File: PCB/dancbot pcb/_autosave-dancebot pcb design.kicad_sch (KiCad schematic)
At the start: 26 parts, among them J1 ESP32-PICO-KIT-V4.1, J2 Voltage Regulator, J4 Pins, J6 Conn_01x04_Socket, J7 Conn_01x04_Socket, Q1 PMOS, Q2 PMOS, Q3 2N3904, Q5 PMOS, SW1 SP switch, SW2 SW_SPST

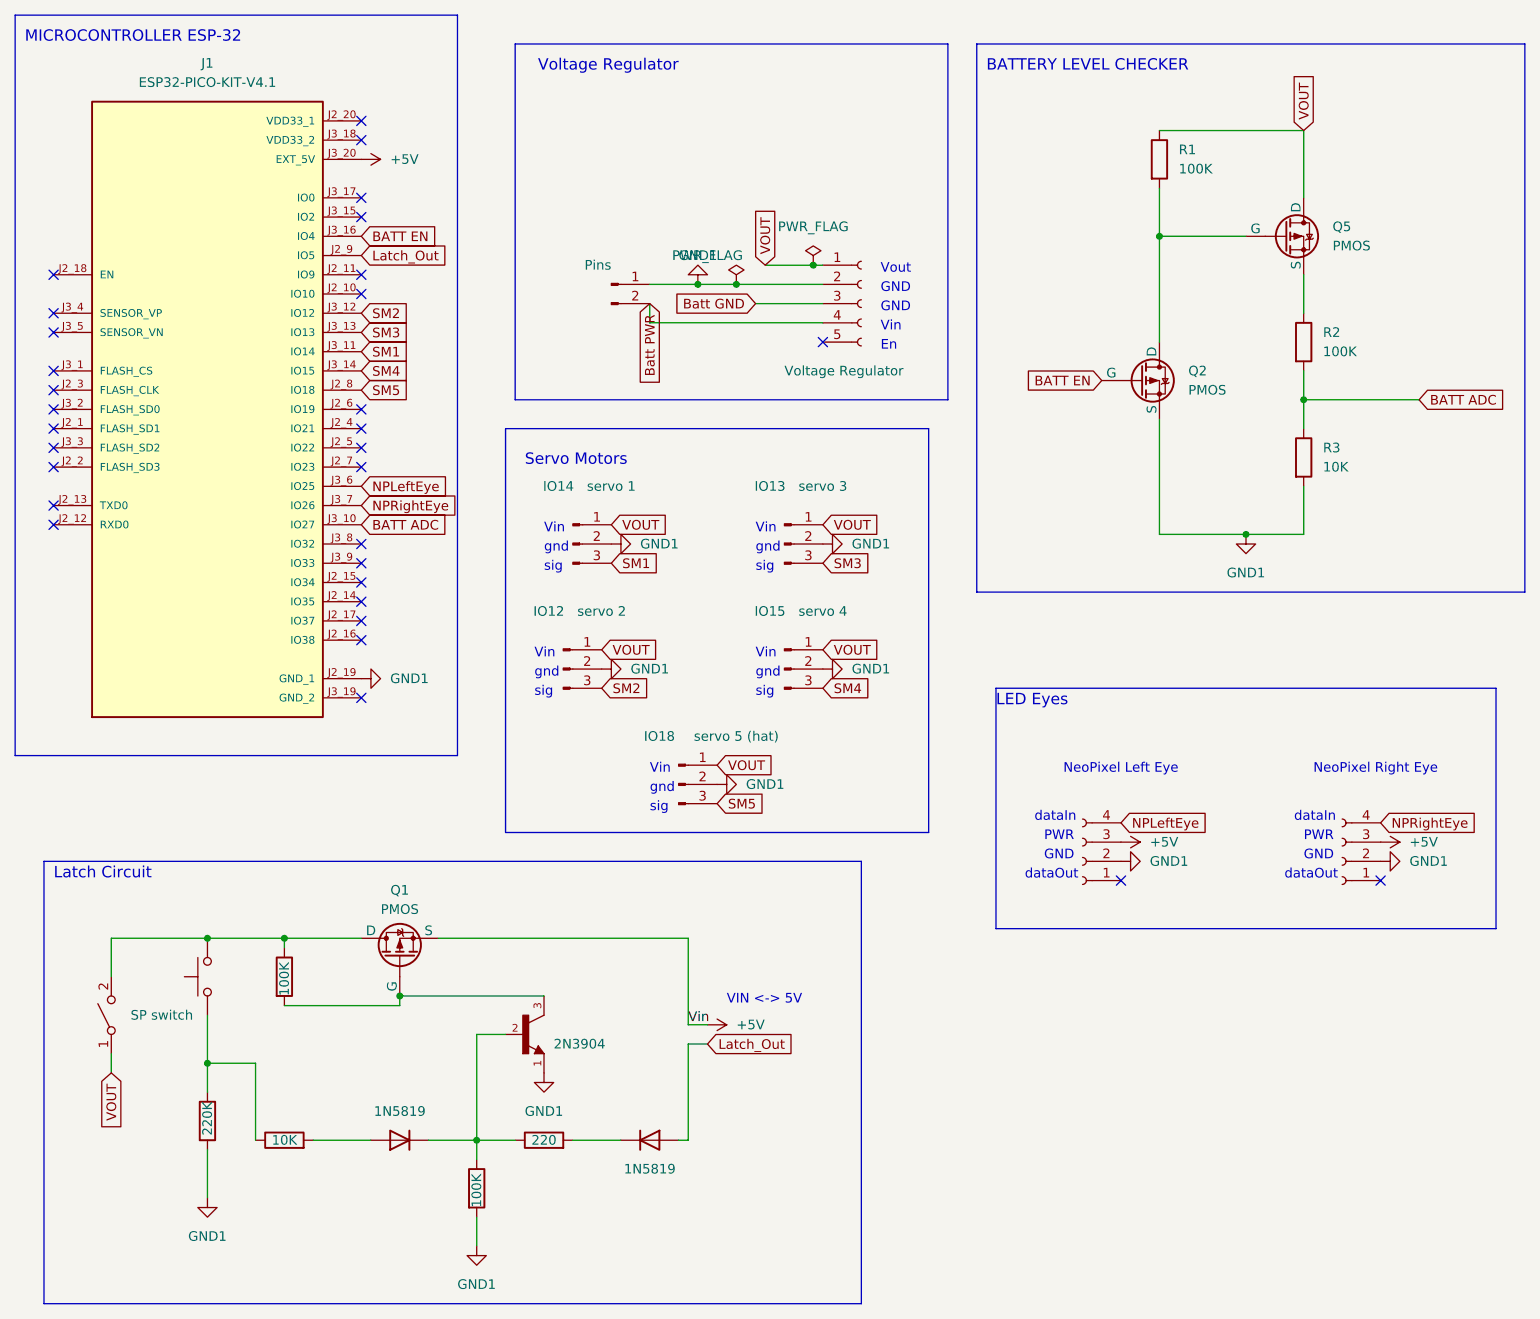
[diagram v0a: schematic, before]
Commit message: Routing rev5, fixed batt lvl checker, fixed gnd plane
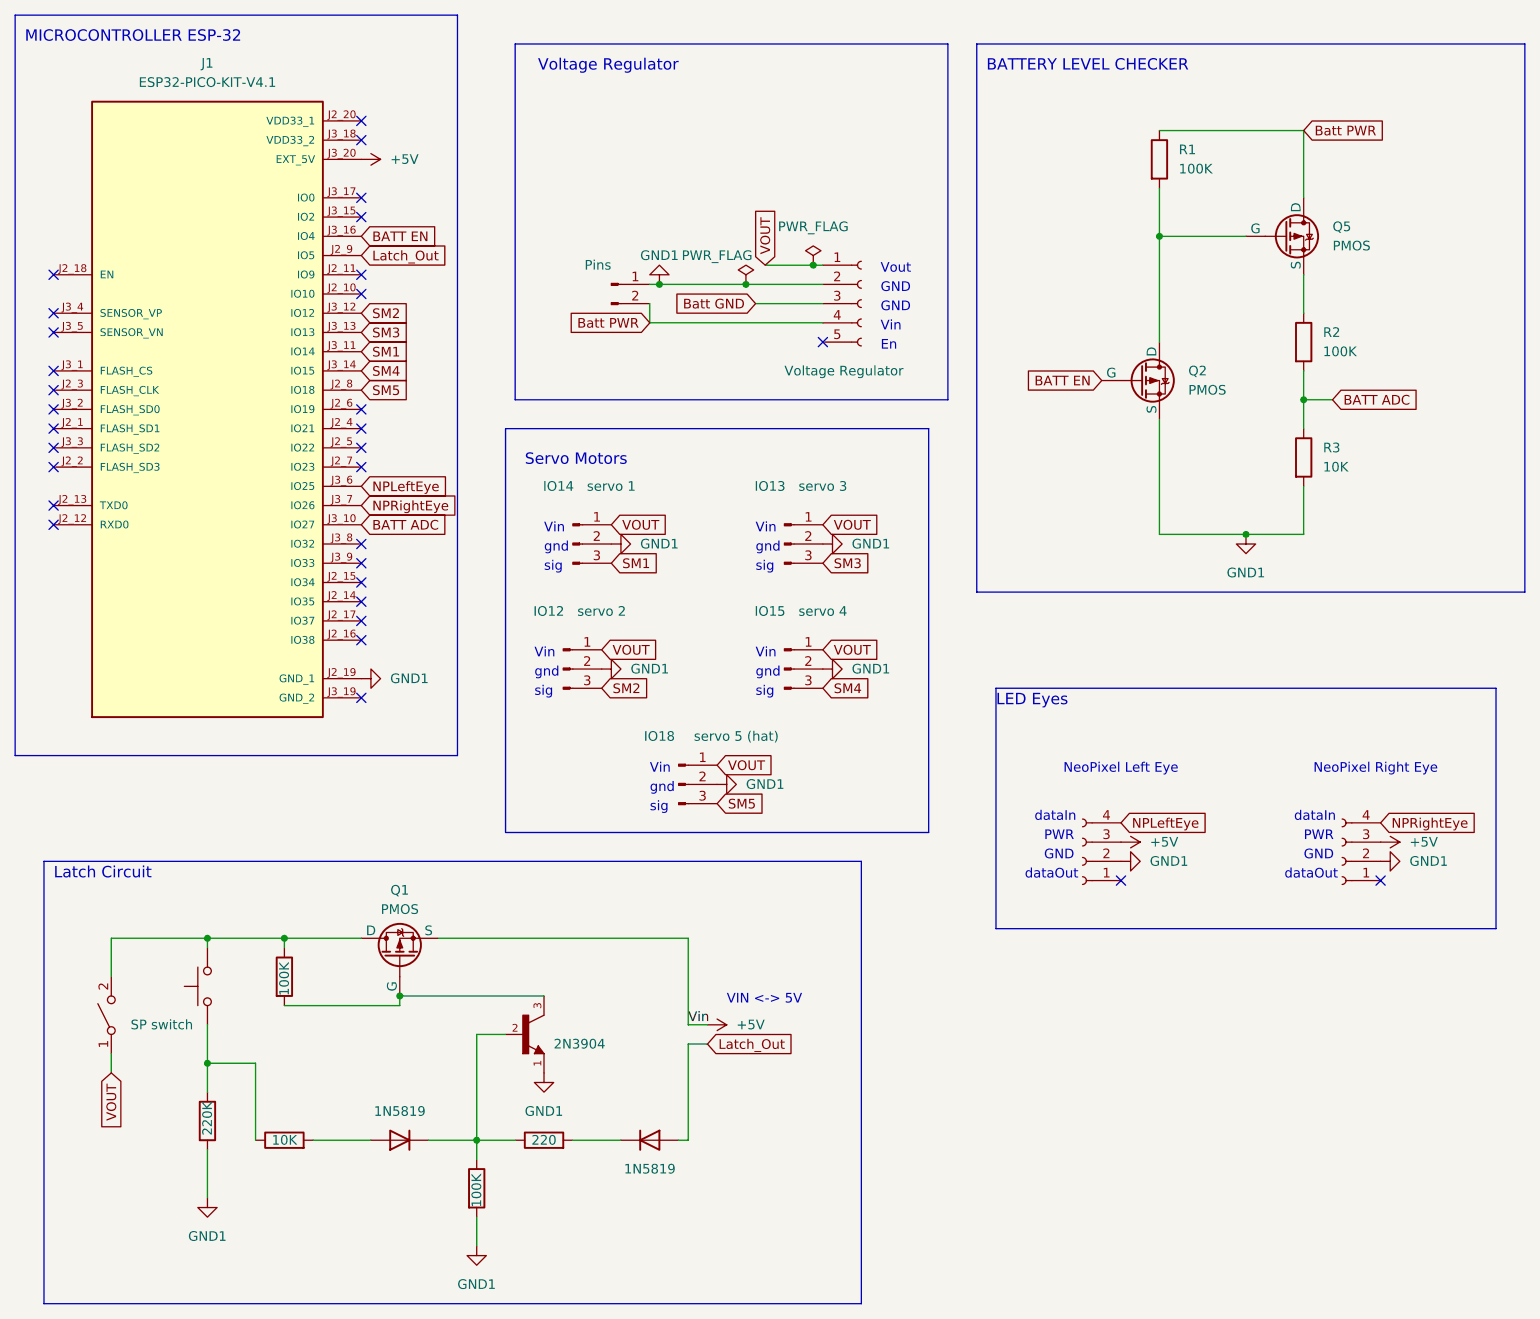
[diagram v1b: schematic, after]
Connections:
- net Batt PWR: now also Q5.1 (D), R1.1
- net VOUT: no longer Q5.1 (D), R1.1
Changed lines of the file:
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@@
 (kicad_sch (version 20230121) (generator eeschema)
   (paper "A4")
-  (junction (at 111.76 50.8) (diameter 0) (color 0 0 0 0)
-  )
   (junction (at 179.07 83.82) (diameter 0) (color 0 0 0 0)
   )
@@
   (junction (at 41.91 153.67) (diameter 0) (color 0 0 0 0)
   )
-  (junction (at 106.68 50.8) (diameter 0) (color 0 0 0 0)
+  (junction (at 113.03 50.8) (diameter 0) (color 0 0 0 0)
+  )
+  (junction (at 101.6 50.8) (diameter 0) (color 0 0 0 0)
   )
   (junction (at 52.07 137.16) (diameter 0) (color 0 0 0 0)
@@
     (stroke (width 0) (type default))
   )
+  (wire (pts (xy 41.91 138.43) (xy 41.91 137.16))
+    (stroke (width 0) (type default))
+  )
   (wire (pts (xy 77.47 163.83) (xy 77.47 149.86))
     (stroke (width 0) (type default))
@@
     (stroke (width 0) (type default))
   )
-  (wire (pts (xy 106.68 50.8) (xy 111.76 50.8))
-    (stroke (width 0) (type default))
-  )
   (wire (pts (xy 41.91 153.67) (xy 48.26 153.67))
     (stroke (width 0) (type default))
@@
     (stroke (width 0) (type default))
   )
+  (wire (pts (xy 113.03 50.8) (xy 123.19 50.8))
+    (stroke (width 0) (type default))
+  )
   (wire (pts (xy 115.57 48.26) (xy 121.92 48.26))
     (stroke (width 0) (type default))
@@
     (stroke (width 0) (type default))
   )
-  (wire (pts (xy 41.91 147.32) (xy 41.91 153.67))
+  (wire (pts (xy 41.91 148.59) (xy 41.91 153.67))
     (stroke (width 0) (type default))
   )
@@
     (stroke (width 0) (type default))
   )
-  (wire (pts (xy 100.33 50.8) (xy 106.68 50.8))
+  (wire (pts (xy 100.33 50.8) (xy 101.6 50.8))
     (stroke (width 0) (type default))
   )
@@
     (stroke (width 0) (type default))
   )
+  (wire (pts (xy 101.6 50.8) (xy 113.03 50.8))
+    (stroke (width 0) (type default))
+  )
   (wire (pts (xy 167.64 83.82) (xy 179.07 83.82))
     (stroke (width 0) (type default))
@@
     (stroke (width 0) (type default))
   )
-  (wire (pts (xy 111.76 50.8) (xy 123.19 50.8))
-    (stroke (width 0) (type default))
-  )
   (wire (pts (xy 167.64 38.1) (xy 167.64 44.45))
     (stroke (width 0) (type default))
@@
     (stroke (width 0) (type default))
   )
-  (wire (pts (xy 186.69 66.04) (xy 201.93 66.04))
+  (wire (pts (xy 186.69 66.04) (xy 190.5 66.04))
     (stroke (width 0) (type default))
   )
@@
     )
   )
-  (global_label "BATT ADC" (shape input) (at 201.93 66.04 0) (fields_autoplaced)
-    (effects (font (size 1.27 1.27)) (justify left))
-    (property "Intersheetrefs" "${INTERSHEET_REFS}" (at 213.8052 66.04 0)
+  (global_label "BATT ADC" (shape input) (at 190.5 66.04 0) (fields_autoplaced)
+    (effects (font (size 1.27 1.27)) (justify left))
+    (property "Intersheetrefs" "${INTERSHEET_REFS}" (at 202.3752 66.04 0)
+      (effects (font (size 1.27 1.27)) (justify left) hide)
+    )
+  )
+  (global_label "Batt PWR" (shape input) (at 186.69 30.48 0) (fields_autoplaced)
+    (effects (font (size 1.27 1.27)) (justify left))
+    (property "Intersheetrefs" "${INTERSHEET_REFS}" (at 198.5046 30.48 0)
       (effects (font (size 1.27 1.27)) (justify left) hide)
     )
@@
     )
   )
-  (global_label "VOUT" (shape input) (at 186.69 30.48 90) (fields_autoplaced)
-    (effects (font (size 1.27 1.27)) (justify left))
-    (property "Intersheetrefs" "${INTERSHEET_REFS}" (at 186.69 22.7776 90)
-      (effects (font (size 1.27 1.27)) (justify left) hide)
-    )
-  )
   (global_label "VOUT" (shape input) (at 115.57 48.26 90) (fields_autoplaced)
     (effects (font (size 1.27 1.27)) (justify left))
@@
     )
   )
-  (global_label "Batt PWR" (shape input) (at 100.33 53.34 270) (fields_autoplaced)
-    (effects (font (size 1.27 1.27)) (justify right))
-    (property "Intersheetrefs" "${INTERSHEET_REFS}" (at 100.33 65.1546 90)
-      (effects (font (size 1.27 1.27)) (justify right) hide)
-    )
-  )
   (global_label "SM1" (shape input) (at 62.23 59.69 0) (fields_autoplaced)
     (effects (font (size 1.27 1.27)) (justify left))
@@
     (effects (font (size 1.27 1.27)) (justify right))
     (property "Intersheetrefs" "${INTERSHEET_REFS}" (at 29.21 162.6424 90)
+      (effects (font (size 1.27 1.27)) (justify right) hide)
+    )
+  )
+  (global_label "Batt PWR" (shape input) (at 100.33 55.88 180) (fields_autoplaced)
+    (effects (font (size 1.27 1.27)) (justify right))
+    (property "Intersheetrefs" "${INTERSHEET_REFS}" (at 88.5154 55.88 0)
       (effects (font (size 1.27 1.27)) (justify right) hide)
     )
@@
     )
   )
-  (symbol (lib_id "power:GND1") (at 106.68 50.8 180) (unit 1)
+  (symbol (lib_id "power:GND1") (at 101.6 50.8 180) (unit 1)
     (in_bom yes) (on_board yes) (dnp no)
-    (property "Reference" "#PWR01" (at 106.68 44.45 0)
-      (effects (font (size 1.27 1.27)) hide)
-    )
-    (property "Value" "GND1" (at 104.14 46.99 0)
+    (property "Reference" "#PWR01" (at 101.6 44.45 0)
+      (effects (font (size 1.27 1.27)) hide)
+    )
+    (property "Value" "GND1" (at 99.06 46.99 0)
       (effects (font (size 1.27 1.27)) (justify right))
     )
-    (property "Footprint" "" (at 106.68 50.8 0)
-      (effects (font (size 1.27 1.27)) hide)
-    )
-    (property "Datasheet" "" (at 106.68 50.8 0)
+    (property "Footprint" "" (at 101.6 50.8 0)
+      (effects (font (size 1.27 1.27)) hide)
+    )
+    (property "Datasheet" "" (at 101.6 50.8 0)
       (effects (font (size 1.27 1.27)) hide)
     )
@@
     )
   )
-  (symbol (lib_id "Switch:SW_Push") (at 41.91 142.24 90) (unit 1)
+  (symbol (lib_id "Switch:SW_Push") (at 41.91 143.51 90) (unit 1)
     (in_bom yes) (on_board yes) (dnp no)
-    (property "Reference" "SW1" (at 43.18 140.97 90)
+    (property "Reference" "SW1" (at 43.18 142.24 90)
       (effects (font (size 1.27 1.27)) (justify right) hide)
     )
-    (property "Value" "SP switch" (at 31.75 147.32 90)
+    (property "Value" "SP switch" (at 31.75 148.59 90)
       (effects (font (size 1.27 1.27)) (justify right))
     )
-    (property "Footprint" "Connector_PinHeader_1.00mm:PinHeader_1x02_P1.00mm_Vertical" (at 36.83 142.24 0)
-      (effects (font (size 1.27 1.27)) hide)
-    )
-    (property "Datasheet" "~" (at 36.83 142.24 0)
+    (property "Footprint" "Connector_PinHeader_1.00mm:PinHeader_1x02_P1.00mm_Vertical" (at 36.83 143.51 0)
+      (effects (font (size 1.27 1.27)) hide)
+    )
+    (property "Datasheet" "~" (at 36.83 143.51 0)
       (effects (font (size 1.27 1.27)) hide)
     )
@@
     )
   )
-  (symbol (lib_id "power:PWR_FLAG") (at 111.76 50.8 0) (unit 1)
+  (symbol (lib_id "power:PWR_FLAG") (at 113.03 50.8 0) (unit 1)
     (in_bom yes) (on_board yes) (dnp no)
-    (property "Reference" "#FLG02" (at 111.76 48.895 0)
-      (effects (font (size 1.27 1.27)) hide)
-    )
-    (property "Value" "PWR_FLAG" (at 107.95 46.99 0)
-      (effects (font (size 1.27 1.27)))
-    )
-    (property "Footprint" "" (at 111.76 50.8 0)
-      (effects (font (size 1.27 1.27)) hide)
-    )
-    (property "Datasheet" "~" (at 111.76 50.8 0)
-      (effects (font (size 1.27 1.27)) hide)
-    )
+    (property "Reference" "#FLG02" (at 113.03 48.895 0)
+      (effects (font (size 1.27 1.27)) hide)
+    )
+    (property "Value" "PWR_FLAG" (at 109.22 46.99 0)
+      (effects (font (size 1.27 1.27)))
+    )
+    (property "Footprint" "" (at 113.03 50.8 0)
+      (effects (font (size 1.27 1.27)) hide)
+    )
+    (property "Datasheet" "~" (at 113.03 50.8 0)
+      (effects (font (size 1.27 1.27)) hide)
+    )
